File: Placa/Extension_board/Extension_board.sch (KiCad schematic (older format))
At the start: 8 parts, among them J1 USB_B_Micro, J2 USB_B_Micro, J3 Conn_01x04_Male, U1 STEVAL-STLCS01V1

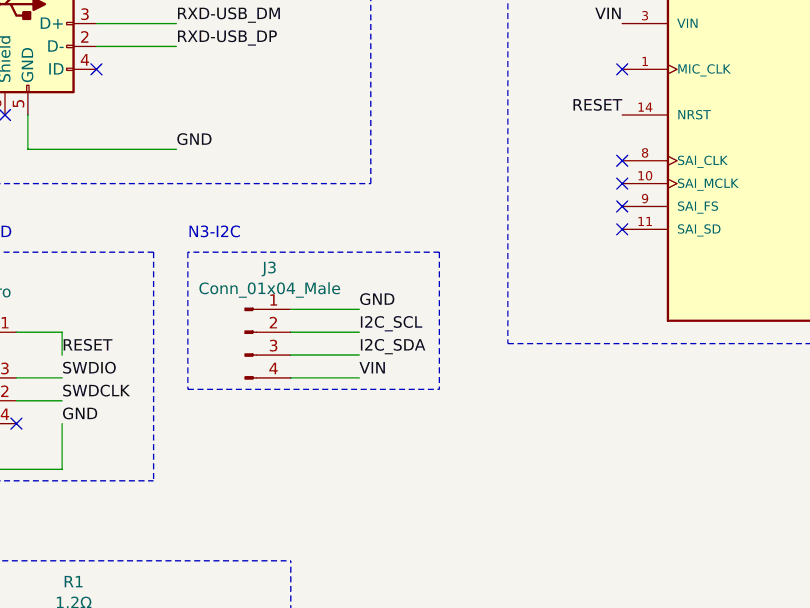
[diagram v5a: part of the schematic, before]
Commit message: Agregado de nuevos pines en I2C
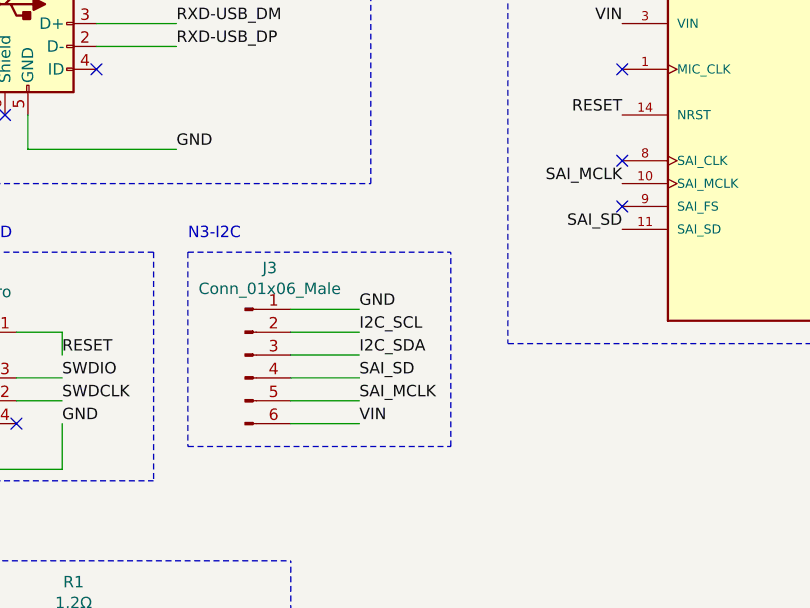
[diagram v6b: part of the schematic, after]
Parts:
- removed J3: Conn_01x04_Male, Connector_PinHeader_2.54mm:PinHeader_1x04_P2.54mm_Horizontal, symbol Connector:Conn_01x04_Male
- added J3: Conn_01x06_Male, Connector_PinHeader_2.54mm:PinHeader_1x06_P2.54mm_Horizontal, symbol Connector:Conn_01x06_Male
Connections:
- net GND: now also J3.1 (Pin_1)
- net I2C_SCL: now also J3.2 (Pin_2)
- net I2C_SDA: now also J3.3 (Pin_3)
- net VIN: now also J3.6 (Pin_6)
- net SAI_MCLK: now reaches U1.10 (SAI_MCLK)
- net SAI_MCLK: now also J3.5 (Pin_5)
- net SAI_SD: now reaches U1.11 (SAI_SD)
- net SAI_SD: now also J3.4 (Pin_4)
- no-connect marks 11 -> 9
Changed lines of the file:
@@
 N4-Regulación
 NoConn ~ 4250 2250
-NoConn ~ 4250 2350
-NoConn ~ 4250 2450
-NoConn ~ 4250 2550
 NoConn ~ 6050 1450
 Text Label 3100 3100 0    50   ~ 0
@@
 Text Label 3100 3000 0    50   ~ 0
 I2C_SCL
-Wire Notes Line
-	3450 2650 2350 2650
 Text Notes 2350 2600 0    50   ~ 0
 N3-I2C
@@
 Text Label 3100 2900 0    50   ~ 0
 GND
-$Comp
-L Connector:Conn_01x04_Male J3
-U 1 1 60C28856
-P 2600 3000
-F 0 "J3" H 2708 3281 50  0000 C CNN
-F 1 "Conn_01x04_Male" H 2708 3190 50  0000 C CNN
-F 2 "Connector_PinHeader_2.54mm:PinHeader_1x04_P2.54mm_Horizontal" H 2600 3000 50  0001 C CNN
-F 3 "~" H 2600 3000 50  0001 C CNN
-	1    2600 3000
-	1    0    0    -1
-$EndComp
 Wire Wire Line
 	2800 2900 3100 2900
@@
 Wire Wire Line
 	2800 3200 3100 3200
-Wire Notes Line
-	2350 3250 3450 3250
-Wire Notes Line
-	2350 2650 2350 3250
-Wire Notes Line
-	3450 2650 3450 3250
 $Comp
 L Connector:USB_B_Micro J2
@@
 Wire Wire Line
 	1200 4300 1700 4300
+Text Label 3100 3400 0    50   ~ 0
+VIN
+$Comp
+L Connector:Conn_01x06_Male J3
+U 1 1 60E39457
+P 2600 3100
+F 0 "J3" H 2708 3481 50  0000 C CNN
+F 1 "Conn_01x06_Male" H 2708 3390 50  0000 C CNN
+F 2 "Connector_PinHeader_2.54mm:PinHeader_1x06_P2.54mm_Horizontal" H 2600 3100 50  0001 C CNN
+F 3 "~" H 2600 3100 50  0001 C CNN
+	1    2600 3100
+	1    0    0    -1
+$EndComp
+Wire Wire Line
+	2800 3300 3100 3300
+Wire Wire Line
+	2800 3400 3100 3400
+Wire Notes Line
+	2350 2650 2350 3500
+Text Label 3100 3300 0    50   ~ 0
+SAI_MCLK
+Text Label 4250 2350 2    50   ~ 0
+SAI_MCLK
+NoConn ~ 4250 2450
+Text Label 4250 2550 2    50   ~ 0
+SAI_SD
 Text Label 3100 3200 0    50   ~ 0
-VIN
+SAI_SD
+Wire Notes Line
+	3500 3500 3500 2650
+Wire Notes Line
+	2350 2650 3500 2650
+Wire Notes Line
+	2350 3500 3500 3500
 $EndSCHEMATC

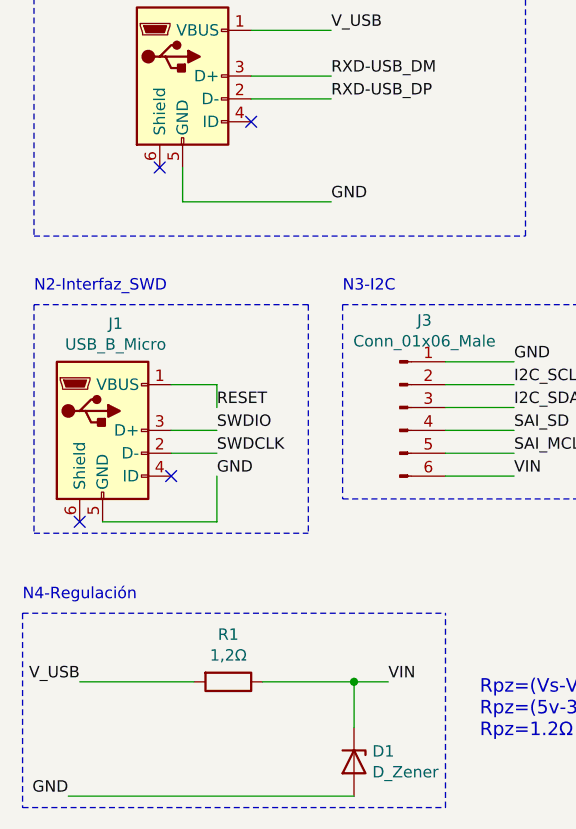
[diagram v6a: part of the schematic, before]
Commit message: Correccion de errores en pads y pistas
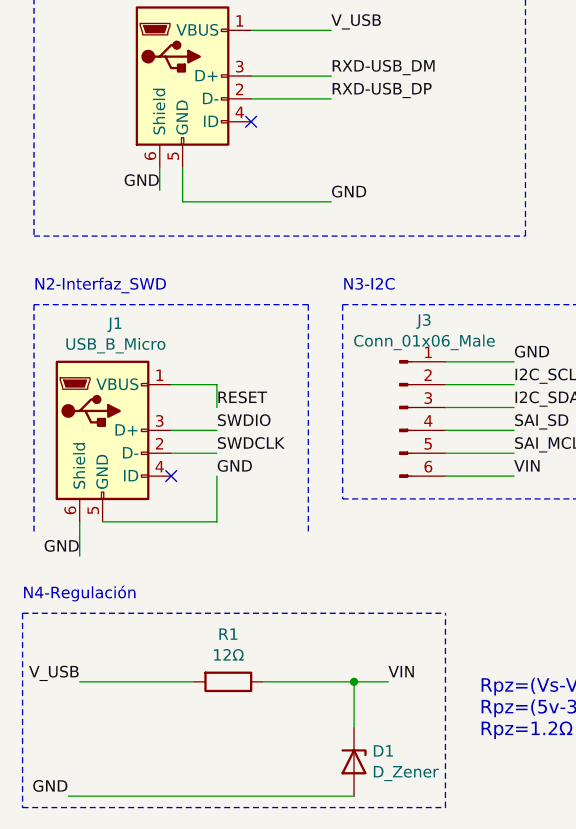
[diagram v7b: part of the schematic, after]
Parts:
- R1: value 1,2Ω -> 12Ω
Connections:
- net GND: now also J1.6 (Shield), J2.6 (Shield)
- no-connect marks 9 -> 7
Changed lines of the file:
@@
 P 1850 4300
 F 0 "R1" V 1643 4300 50  0000 C CNN
-F 1 "1,2Ω" V 1734 4300 50  0000 C CNN
+F 1 "12Ω" V 1734 4300 50  0000 C CNN
 F 2 "Resistor_THT:R_Axial_DIN0207_L6.3mm_D2.5mm_P7.62mm_Horizontal" V 1780 4300 50  0001 C CNN
 F 3 "~" H 1850 4300 50  0001 C CNN
@@
 Wire Wire Line
 	1650 2050 1650 2200
-NoConn ~ 1550 2050
 NoConn ~ 4250 1850
-NoConn ~ 1950 1850
 Wire Notes Line
 	1000 2350 3150 2350
@@
 	1800 3600 1800 3400
 NoConn ~ 1600 3400
-NoConn ~ 1200 3600
-Wire Notes Line
-	1000 3650 2200 3650
 Wire Notes Line
 	1000 2650 1000 3650
@@
 Wire Notes Line
 	2350 3500 3500 3500
+NoConn ~ 1950 1850
+Text Label 1550 2150 2    50   ~ 0
+GND
+Wire Wire Line
+	1550 2050 1550 2150
+Text Label 1200 3750 2    50   ~ 0
+GND
+Wire Wire Line
+	1200 3600 1200 3750
 $EndSCHEMATC

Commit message: Revision
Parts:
- added C1: C, Capacitor_SMD:C_0805_2012Metric, symbol Device:C
- added SW1: SW_PUSHBUTTON, Button_Switch_THT:SW_PUSH_6mm_H5mm, symbol freetronics_schematic:SW_PUSHBUTTON
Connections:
- net GND: now also C1.2, SW1.1
- net RESET: now also C1.1, SW1.2
- net RXD-USB_DM: now also J2.2 (D-); no longer J2.3 (D+)
- net RXD-USB_DP: now also J2.3 (D+); no longer J2.2 (D-)
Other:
- note added: "N7-Reset"
- moved on the sheet: D1, D2, R1, R4
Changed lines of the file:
@@
 VIN
 NoConn ~ 6050 1650
+Text Label 2300 1750 0    50   ~ 0
+RXD-USB_DM
 Text Label 2300 1650 0    50   ~ 0
-RXD-USB_DM
-Text Label 2300 1750 0    50   ~ 0
 RXD-USB_DP
 Wire Wire Line
@@
 L Device:D_Zener D1
 U 1 1 60BFFB26
-P 2400 4650
-F 0 "D1" V 2354 4730 50  0000 L CNN
-F 1 "D_Zener" V 2445 4730 50  0000 L CNN
-F 2 "Resistor_THT:R_Axial_DIN0207_L6.3mm_D2.5mm_P5.08mm_Vertical" H 2400 4650 50  0001 C CNN
-F 3 "~" H 2400 4650 50  0001 C CNN
-	1    2400 4650
+P 2400 4700
+F 0 "D1" V 2354 4780 50  0000 L CNN
+F 1 "D_Zener" V 2445 4780 50  0000 L CNN
+F 2 "Resistor_THT:R_Axial_DIN0207_L6.3mm_D2.5mm_P5.08mm_Vertical" H 2400 4700 50  0001 C CNN
+F 3 "~" H 2400 4700 50  0001 C CNN
+	1    2400 4700
 	0    1    1    0
 $EndComp
-Text Label 1200 4300 2    50   ~ 0
+Text Label 1200 4350 2    50   ~ 0
 V_USB
-Text Label 1150 4800 2    50   ~ 0
-GND
-Text Label 2550 4300 0    50   ~ 0
+Text Label 1150 4850 2    50   ~ 0
+GND
+Text Label 2550 4350 0    50   ~ 0
 VIN
 $Comp
 L Device:R R1
 U 1 1 60C00A3D
-P 1850 4300
-F 0 "R1" V 1643 4300 50  0000 C CNN
-F 1 "12Ω" V 1734 4300 50  0000 C CNN
-F 2 "Resistor_THT:R_Axial_DIN0207_L6.3mm_D2.5mm_P7.62mm_Horizontal" V 1780 4300 50  0001 C CNN
-F 3 "~" H 1850 4300 50  0001 C CNN
-	1    1850 4300
+P 1850 4350
+F 0 "R1" V 1643 4350 50  0000 C CNN
+F 1 "12Ω" V 1734 4350 50  0000 C CNN
+F 2 "Resistor_THT:R_Axial_DIN0207_L6.3mm_D2.5mm_P7.62mm_Horizontal" V 1780 4350 50  0001 C CNN
+F 3 "~" H 1850 4350 50  0001 C CNN
+	1    1850 4350
 	0    1    1    0
 $EndComp
-Text Notes 950  3950 0    50   ~ 0
+Text Notes 950  4000 0    50   ~ 0
 N4-Regulación
 NoConn ~ 4250 2250
@@
 N3-I2C
 Wire Wire Line
-	1150 4800 2400 4800
-Wire Wire Line
-	2400 4500 2400 4300
-Wire Wire Line
-	2400 4300 2550 4300
-Wire Notes Line
-	950  4000 950  4850
-Wire Notes Line
-	950  4850 2800 4850
-Wire Notes Line
-	2800 4850 2800 4000
-Wire Notes Line
-	950  4000 2800 4000
+	1150 4850 2400 4850
+Wire Wire Line
+	2400 4550 2400 4350
+Wire Wire Line
+	2400 4350 2550 4350
+Wire Notes Line
+	950  4050 950  4900
+Wire Notes Line
+	950  4900 2800 4900
+Wire Notes Line
+	2800 4900 2800 4050
+Wire Notes Line
+	950  4050 2800 4050
 Text Label 3100 2900 0    50   ~ 0
 GND
@@
 Wire Wire Line
 	1650 2200 2300 2200
-Text Notes 2950 4550 0    59   ~ 0
+Text Notes 2950 4600 0    59   ~ 0
 Rpz=(Vs-Vz)/((Iz*1.1)+Il+Ii2c)\nRpz=(5v-3.3v)/(53mA*1.1+100mA+150mA)\nRpz=1.2Ω
 $Comp
 L Device:LED D2
 U 1 1 60C6CD3B
-P 2000 5400
-F 0 "D2" H 1993 5145 50  0000 C CNN
-F 1 "LED" H 1993 5236 50  0000 C CNN
-F 2 "LED_THT:LED_D5.0mm_IRBlack" H 2000 5400 50  0001 C CNN
-F 3 "~" H 2000 5400 50  0001 C CNN
-	1    2000 5400
+P 2000 5450
+F 0 "D2" H 1993 5195 50  0000 C CNN
+F 1 "LED" H 1993 5286 50  0000 C CNN
+F 2 "LED_THT:LED_D5.0mm_IRBlack" H 2000 5450 50  0001 C CNN
+F 3 "~" H 2000 5450 50  0001 C CNN
+	1    2000 5450
 	-1   0    0    1
 $EndComp
@@
 L Device:R R4
 U 1 1 60C6E1B1
-P 1450 5400
-F 0 "R4" V 1243 5400 50  0000 C CNN
-F 1 "1kΩ" V 1334 5400 50  0000 C CNN
-F 2 "Resistor_THT:R_Axial_DIN0207_L6.3mm_D2.5mm_P7.62mm_Horizontal" V 1380 5400 50  0001 C CNN
-F 3 "~" H 1450 5400 50  0001 C CNN
-	1    1450 5400
+P 1450 5450
+F 0 "R4" V 1243 5450 50  0000 C CNN
+F 1 "1kΩ" V 1334 5450 50  0000 C CNN
+F 2 "Resistor_THT:R_Axial_DIN0207_L6.3mm_D2.5mm_P7.62mm_Horizontal" V 1380 5450 50  0001 C CNN
+F 3 "~" H 1450 5450 50  0001 C CNN
+	1    1450 5450
 	0    1    1    0
 $EndComp
-Text Label 2400 5400 0    50   ~ 0
-GND
-Wire Wire Line
-	2150 5400 2400 5400
-Wire Wire Line
-	1600 5400 1850 5400
-Text Label 1300 5400 2    50   ~ 0
+Text Label 2400 5450 0    50   ~ 0
+GND
+Wire Wire Line
+	2150 5450 2400 5450
+Wire Wire Line
+	1600 5450 1850 5450
+Text Label 1300 5450 2    50   ~ 0
 V_USB
 Wire Notes Line
-	2600 5100 950  5100
-Text Notes 1000 5050 0    50   ~ 0
+	2600 5150 950  5150
+Text Notes 1000 5100 0    50   ~ 0
 N5-LEDs
 $Comp
@@
 $EndComp
 Wire Notes Line
-	950  5100 950  5500
-Wire Notes Line
-	950  5500 2600 5500
-Wire Notes Line
-	2600 5500 2600 5100
+	950  5150 950  5550
+Wire Notes Line
+	950  5550 2600 5550
+Wire Notes Line
+	2600 5550 2600 5150
 Wire Wire Line
 	1600 3000 1800 3000
@@
 Wire Wire Line
 	1800 3600 1800 3400
-NoConn ~ 1600 3400
-Wire Notes Line
-	1000 2650 1000 3650
-Wire Notes Line
-	2200 2650 2200 3650
-Wire Wire Line
-	2000 4300 2400 4300
-Connection ~ 2400 4300
-Wire Wire Line
-	1200 4300 1700 4300
+Wire Wire Line
+	2000 4350 2400 4350
+Connection ~ 2400 4350
+Wire Wire Line
+	1200 4350 1700 4350
 Text Label 3100 3400 0    50   ~ 0
 VIN
@@
 Wire Notes Line
 	2350 3500 3500 3500
-NoConn ~ 1950 1850
 Text Label 1550 2150 2    50   ~ 0
 GND
@@
 Wire Wire Line
 	1200 3600 1200 3750
+Wire Notes Line
+	1000 2650 1000 3800
+Wire Notes Line
+	1000 3800 2200 3800
+Wire Notes Line
+	2200 3800 2200 2650
+$Comp
+L freetronics_schematic:SW_PUSHBUTTON SW1
+U 1 1 610BD908
+P 1450 6150
+F 0 "SW1" H 1450 6415 50  0000 C CNN
+F 1 "SW_PUSHBUTTON" H 1450 6324 50  0000 C CNN
+F 2 "Button_Switch_THT:SW_PUSH_6mm_H5mm" H 1450 6150 60  0001 C CNN
+F 3 "" H 1450 6150 60  0000 C CNN
+	1    1450 6150
+	1    0    0    -1
+$EndComp
+$Comp
+L Device:C C1
+U 1 1 610BE494
+P 1750 6500
+F 0 "C1" H 1865 6546 50  0000 L CNN
+F 1 "C" H 1865 6455 50  0000 L CNN
+F 2 "Capacitor_SMD:C_0805_2012Metric" H 1788 6350 50  0001 C CNN
+F 3 "~" H 1750 6500 50  0001 C CNN
+	1    1750 6500
+	1    0    0    -1
+$EndComp
+Wire Wire Line
+	1750 6150 1750 6350
+Wire Wire Line
+	1750 6650 1150 6650
+Wire Wire Line
+	1150 6650 1150 6150
+Text Label 1150 6850 2    50   ~ 0
+GND
+Wire Wire Line
+	1150 6650 1150 6850
+Connection ~ 1150 6650
+Text Label 2000 6150 0    50   ~ 0
+RESET
+Wire Wire Line
+	1750 6150 2000 6150
+Connection ~ 1750 6150
+Wire Notes Line
+	950  5850 950  6900
+Wire Notes Line
+	950  6900 2300 6900
+Wire Notes Line
+	2300 6900 2300 5850
+Wire Notes Line
+	2300 5850 950  5850
+Text Notes 950  5850 0    50   ~ 0
+N7-Reset
+NoConn ~ 1950 1850
+NoConn ~ 1600 3400
 $EndSCHEMATC
